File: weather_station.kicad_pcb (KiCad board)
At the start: 2 copper layers, 24 x 57.8 mm, 73 parts, among them J1 Conn_01x03, J2 Conn_01x05_Male, J3 Conn_01x05, J4 Conn_02x04_Odd_Even, J5 USB_B_Micro, P1 USB_C_Plug, Q1 BSS138, Q2 BSS84, Q3 BSS84, Q4 BSS138_NC, Q5 BSS138, SW1 SW_Push, U1 ESP-12F, U2 AMS1117-3.3, U3 LM75B, U4 BME280, U5 BME680

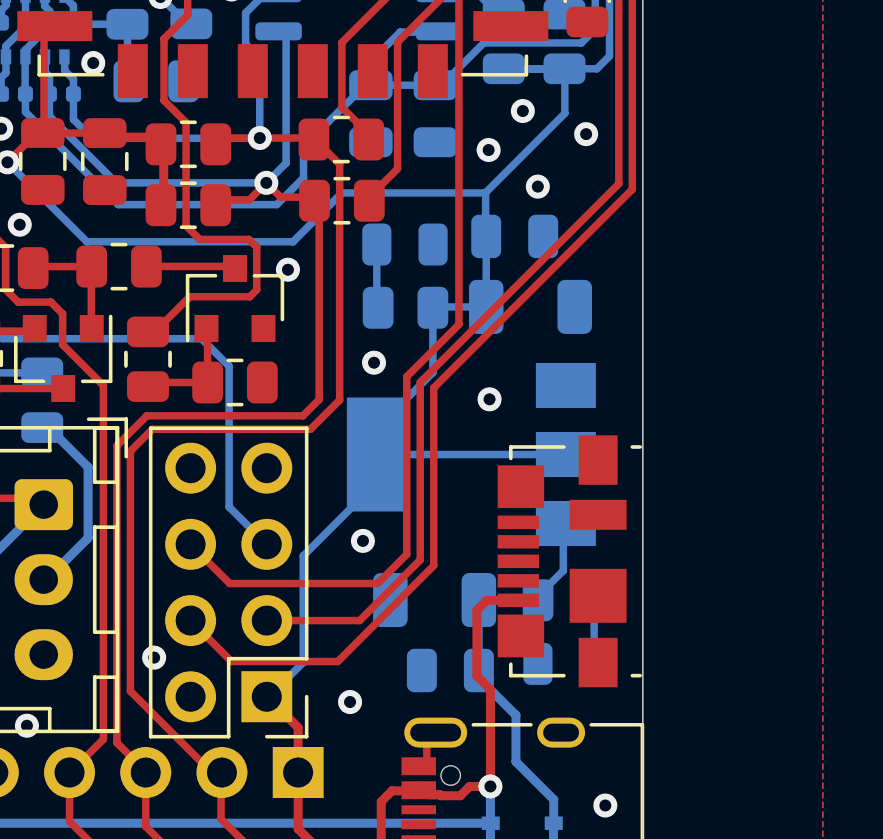
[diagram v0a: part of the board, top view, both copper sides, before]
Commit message: edit silkscreen
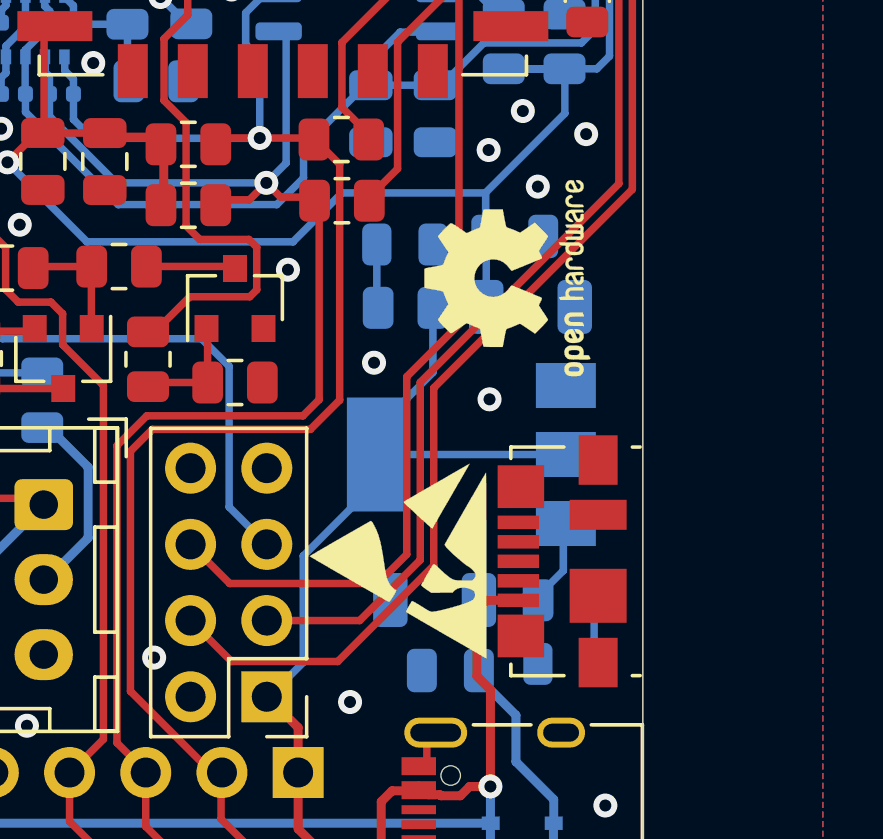
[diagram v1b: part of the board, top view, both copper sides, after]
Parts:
- added REF**: ESD-Logo_6.6x6mm_SilkScreen, Symbol:ESD-Logo_6.6x6mm_SilkScreen, F.Cu at (153.8, 120.9)
- added REF**: OSHW-Logo2_7.3x6mm_SilkScreen, Symbol:OSHW-Logo2_7.3x6mm_SilkScreen, F.Cu at (157.5, 111.5)
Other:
- board text added: "github.com: mec-kon/weather_station eike2511/ hrahlf/"

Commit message: added gerber and drill files
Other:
- board text added: "BOT"
- board text added: "TOP"
